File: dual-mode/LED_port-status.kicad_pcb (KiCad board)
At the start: 2 copper layers, 23.7 x 12.5 mm, 21 parts, among them P1 CONN_9

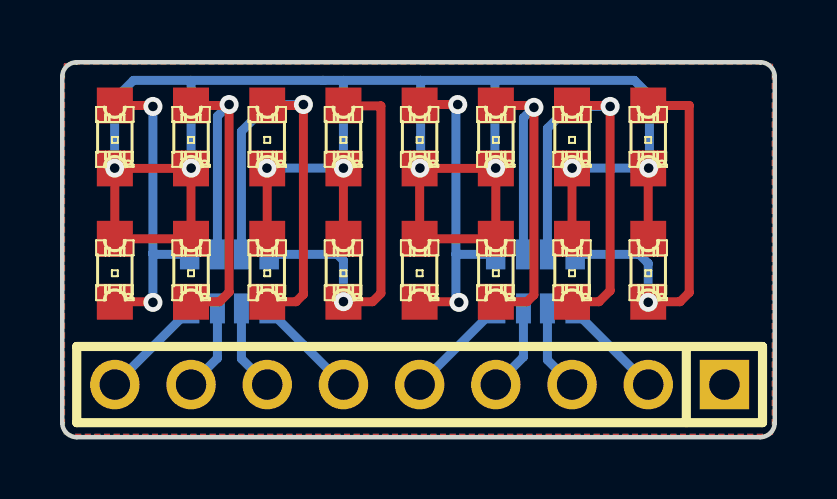
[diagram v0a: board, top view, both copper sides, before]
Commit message: Updated 'dual-mode'.
* multi-footprints 0402-0603-0805
* silkscreen tweaks
* mask tweaks
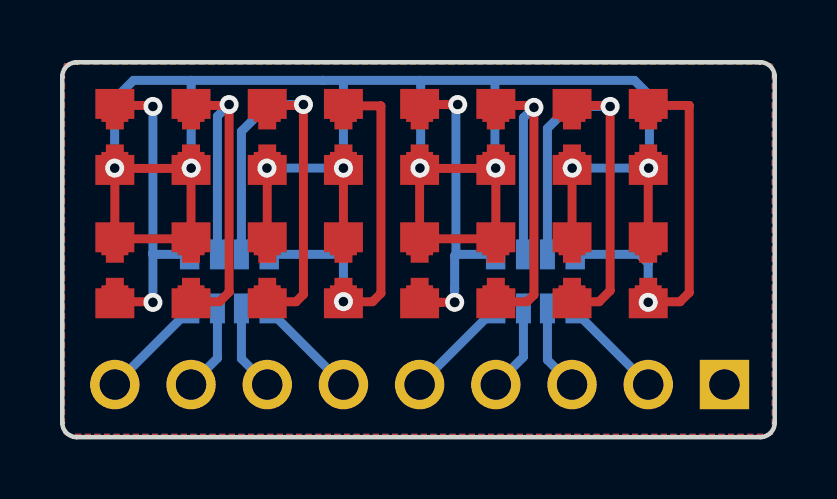
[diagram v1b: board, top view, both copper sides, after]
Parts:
- D1, D10, D11, D12, D13, D14, D15, D16, D2, D3, D4, D5, D6, D7, D8, D9: footprint LED-0805 -> my_parts:R_0805_0603_0402
- moved G1 1.00 mm to (101.4, 82.5)
- moved G2 1.00 mm to (81.4, 82.5)
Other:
- board text added: "LED_port-status V0.21.b 2015 - blog.spitzenpfeil.org"
- board text added: "Oh, shiny!"
- board text removed: "LED_port-status V0.21 2013 - blog.spitzenpfeil.org"
- board text removed: "Make my day"
- board text removed: "More light!"
